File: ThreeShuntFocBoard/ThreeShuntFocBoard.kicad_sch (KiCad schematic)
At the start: 178 parts, among them J1 Conn_01x05, J10 Conn_01x01, J11 Conn_01x01, J12 Conn_01x01, J13 Conn_01x01, J14 Conn_01x01, J15 Conn_01x01, J16 Conn_01x01, J17 Conn_01x01, J18 Conn_01x01, J2 Conn_01x01, J3 Conn_01x03, J5 Conn_01x05, J6 Conn_01x01, J7 Conn_02x03_Odd_Even, J8 Conn_01x01, J9 Conn_01x01, Q1 MMBT5551L, Q10 IRF540N, Q11 MMBT5551L, Q12 SS8050, Q13 SS8550, Q14 SS8550, Q15 SS8550, Q16 SS8550, Q17 IRF540N, Q18 IRF540N, Q19 IRF540N, Q2 SS8050, Q20 IRF540N, Q21 MMBT5551L, Q22 SS8050, Q23 SS8550, Q24 SS8550, Q25 SS8550, Q26 SS8550, Q27 IRF540N, Q28 IRF540N, Q29 IRF540N, Q3 SS8550, Q30 IRF540N, Q31 AOD2146, Q4 SS8550, Q5 SS8550, Q6 SS8550, Q7 IRF540N, Q8 IRF540N, Q9 IRF540N, U1 TX4131L_ESOP8, U2 AMS1117

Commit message: Only PhaseA inverter section is implemented : need to review
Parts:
- removed C1, C11, C17, C9: 100nF, Footprints:C_0603, symbol Device:C_Small
- removed C10, C14, C20: 47uF 63V, BLDC:220uF63V, symbol Device:C_Polarized_US
- removed C12, C13, C18, C19, C4, C5, C6, C7, C8: 10nF, Footprints:C_0603, symbol Device:C_Small
- removed C15, C21: 220uF 80V, Footprints:220uF_80VDC, symbol Device:C_Polarized_US
- removed C16, C22, C31: 104J 100V, Footprints:104J_100V, symbol Device:C
- removed C2, C3: 470uF 80V, Footprints:220uF_80VDC, symbol Device:C_Polarized_US
- removed C23: 47uF 160V_UVR2C470MHD1TO, Footprints:47uF_25V, symbol Device:C_Polarized_US
- removed C24: 100nF_200V, Footprints:0.1uF200V, symbol Device:C_Small
- removed C25: 2.2uF_0805, Footprints:1206_C, symbol Device:C_Small
- removed C26: 4.7uF 25V, Footprints:C_0603, symbol Device:C_Small
- removed C27: 220uF 25V, Footprints:220uF 25V, symbol Device:C_Polarized_US
- removed C28: 100nF 25V, Footprints:C_0603, symbol Device:C_Small
- removed C29: 100uF 25V, Footprints:100uF 25V_2917, symbol Device:C_Polarized_US
- removed C30: 22uF 10V, Footprints:22uF 10V, symbol Device:C_Polarized_US
- removed D1, D4, D7: 1N4007, BLDC:ZenerDiode_S1M, symbol Diode:1N4007
- removed D10: BZT52C15-13-F, Footprints:BZT52C15-13-F, symbol Diode:BZT52Bxx
- removed D11: 1N4148W-7-F_SOD123, Footprints:SOD_123_v1, symbol Diode:1N4148
- removed D12, D13: D_Schottky, Footprints:SS24-HF, symbol Device:D_Schottky
- removed D14, D15: LED, Footprints:LED_0603, symbol Device:LED
- removed D2, D3, D5, D6, D8, D9: 1N4148, Footprints:SOD_123_v1, symbol Diode:1N4148
- removed FB1: FerriteBead, Footprints:BLM21SP471SN1D, symbol Device:FerriteBead
- removed FB2, FB3, FB4: BLM21SP471SN1D, Footprints:BLM21SP471SN1D, symbol Device:FerriteBead
- removed J1, J5: Conn_01x05, BLDC:Socket_Strip_Straight_1x05_Pitch2.54mm, symbol Connector_Generic:Conn_01x05
- removed J10, J11, J12, J13, J14, J15, J16, J17, J18, J2, J6, J8, J9: Conn_01x01, Footprints:Powe_pad, symbol Connector_Generic:Conn_01x01
- removed J3: Conn_01x03, BLDC:Socket_Strip_Straight_1x03_Pitch2.54mm, symbol Connector_Generic:Conn_01x03
- removed J7: Conn_02x03_Odd_Even, BLDC:Socket_Strip_Straight_oddeven_2x06_Pitch2.54mm, symbol Connector_Generic:Conn_02x03_Odd_Even
- removed JP1, JP2: Jumper_2_Open, Footprints:104J_100V, symbol Jumper:Jumper_2_Open
- removed L1: Fixed Inductors 47uH, Footprints:47uH_Inductor, symbol Device:L
- removed Q1, Q11, Q21: MMBT5551L, Footprints:SOT-23_v1, symbol Transistor_BJT:MMBT5551L
- removed Q10, Q17, Q18, Q19, Q20, Q27, Q28, Q29, Q30, Q7, Q8, Q9: IRF540N, BLDC:TO-220-3_Vertical, symbol Transistor_FET:IRF540N
- removed Q12, Q2, Q22: SS8050, Footprints:SOT-23_v1, symbol Transistor_BJT:S8050
- removed Q13, Q14, Q15, Q16, Q23, Q24, Q25, Q26, Q3, Q4, Q5, Q6: SS8550, Footprints:SOT-23_v1, symbol Transistor_BJT:S8550
- removed Q31: AOD2146, Footprints:AOD4126, symbol Transistor_FET:IRF540N
- removed R1, R25, R5: 0E, Footprints:R_0603, symbol Device:R
- removed R10, R12, R32, R34, R52, R54: 510E, Footprints:R_0603, symbol Device:R
- removed R11, R13, R17, R18, R2, R27, R28, R29, R3, R30, R31, R33, R35, R36, R37, R4, R45, R46, R48, R49, R50, R51, R53, R55, R56, R57, R6, R7, R8, R9: 2.2K, Footprints:R_0603, symbol Device:R
- removed R14, R15, R16: 3.3K, Footprints:R_0603, symbol Device:R
- removed R19, R38, R58: 560R, Footprints:R_0603, symbol Device:R
- removed R20, R39, R59: 560E, Footprints:R_0603, symbol Device:R
- removed R21, R22, R23, R24, R40, R41, R42, R43, R60, R61, R62, R63: 6.9E, Footprints:R_0603, symbol Device:R
- removed R26, R44, R64: 10K, Footprints:1206_R, symbol Device:R
- removed R47: 51K, Footprints:1206_R, symbol Device:R
- removed R65: 100R, Footprints:R_0603, symbol Device:R
- removed R66, R68: 1.8K, Footprints:R_0603, symbol Device:R
- removed R67, R69: 56K, Footprints:R_0603, symbol Device:R
- removed R70, R71, R72: 0.1R 0.25W, Footprints:0.1R 0.25W, symbol Device:R
- removed R73: 22K, Footprints:R_0603, symbol Device:R
- removed R74: 1.69K, Footprints:R_0603, symbol Device:R
- removed R75: 1K, Footprints:R_0603, symbol Device:R
- removed U1: TX4131L_ESOP8, Footprints:TX4131L_ESOP8, symbol Symbol_lib:TX4131L_ESOP8
- removed U2: AMS1117, Footprints:AMS1117 SOT-223, symbol Regulator_Linear:AMS1117
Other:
- added sheet DigitalSection (DigitalSection.kicad_sch)
- added sheet PhaseA (Inverter.kicad_sch)
- added sheet PowerSupply (PowerSupply.kicad_sch)
- note removed: "+12VDC Supply"
- note removed: "+5VDC Supply"
- note removed: "10KOhm_1 1206"
- note removed: "CHOKE KIND OF CAPACITOR"
- note removed: "DIGITAL_ GND"
- note removed: "INVERTER_SECTION"
- note removed: "PWM SINGALS"
- note removed: "Place this capacitor near to phaseA DRAIN Side"
- note removed: "SUPPLY_CONNECTION"
- note removed: "Test-point"

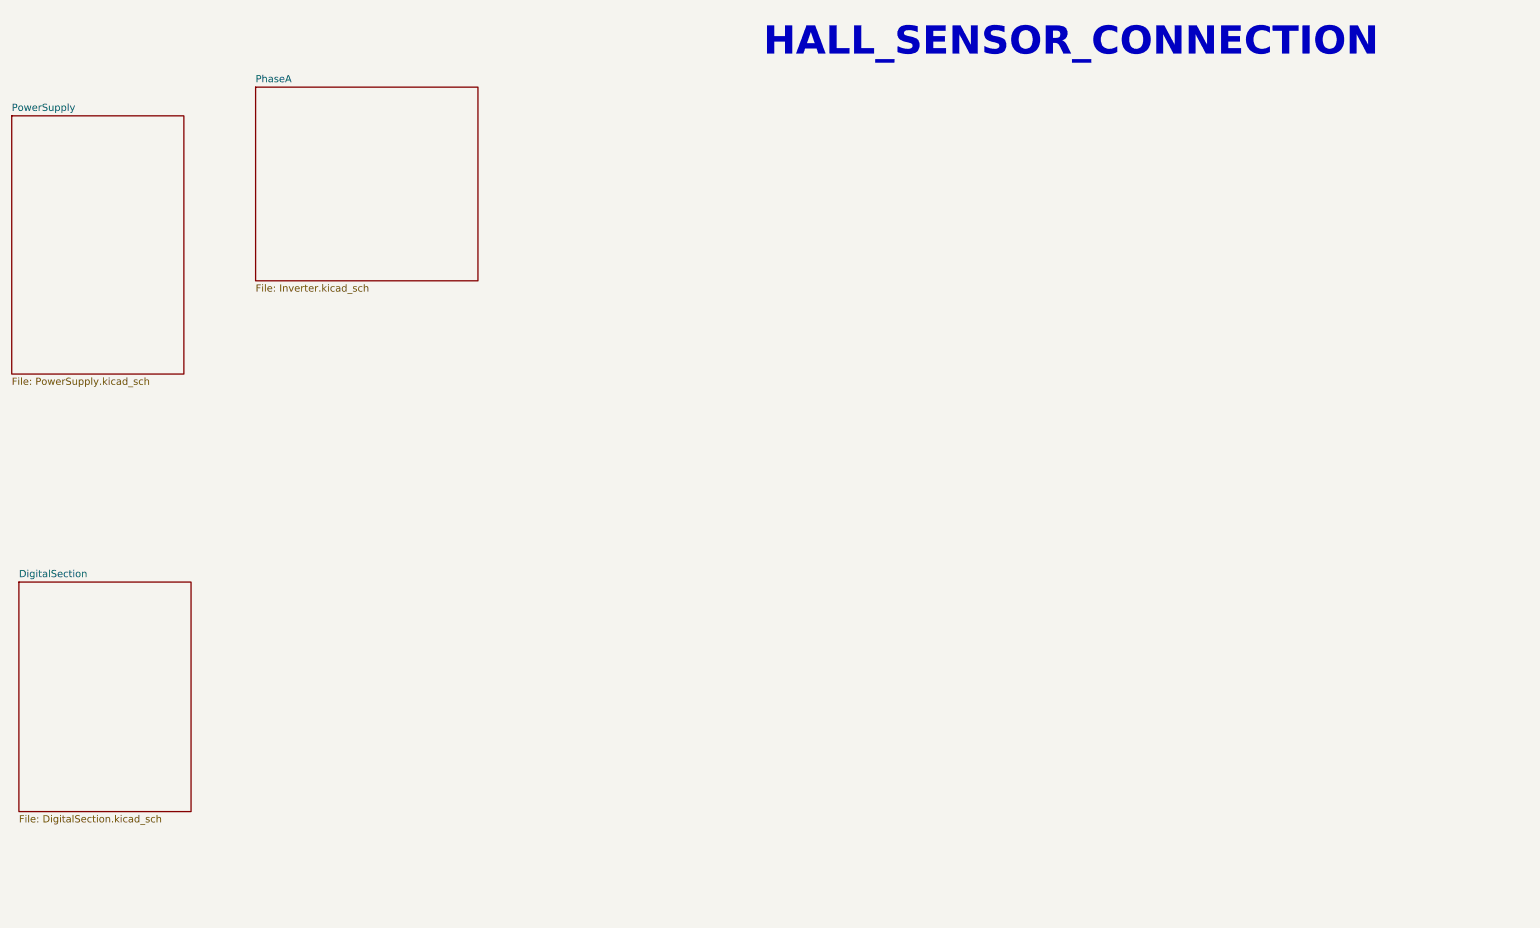
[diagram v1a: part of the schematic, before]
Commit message: commit 2:  Updated Power Supply, Safety Fuse, Phase Design, and Hall Sensor Circuit
for more details read ChangesDetial.txt in same folder.
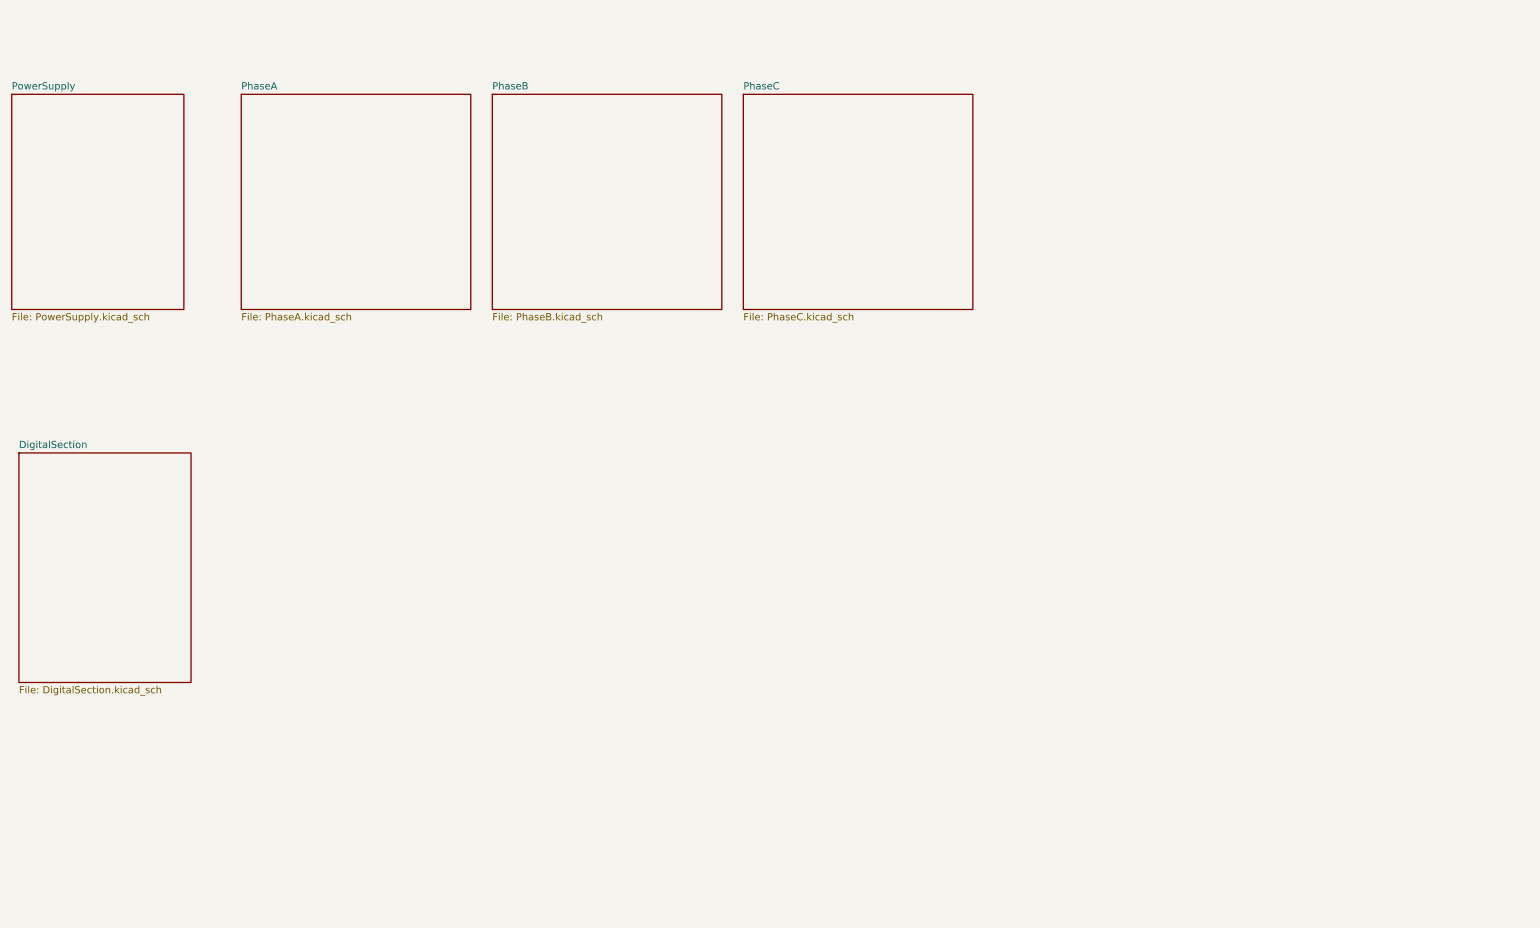
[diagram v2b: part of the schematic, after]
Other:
- added sheet PhaseB (PhaseB.kicad_sch)
- added sheet PhaseC (PhaseC.kicad_sch)
- sheet PhaseA: file Inverter.kicad_sch -> PhaseA.kicad_sch
- note removed: "HALL_SENSOR_CONNECTION"
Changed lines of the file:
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@@
-		)
-	)
-	(text "HALL_SENSOR_CONNECTION"
-		(exclude_from_sim no)
-		(at 157.226 24.13 0)
-		(effects
-			(font
-				(size 5 5)
-				(bold yes)
-			)
-			(justify left bottom)
 		)
 	)
 	(sheet
-		(at 67.31 29.21)
-		(size 39.37 34.29)
+		(at 109.22 30.48)
+		(size 40.64 38.1)
 		(fields_autoplaced yes)
 		(stroke
@@
 			(color 0 0 0 0.0000)
 		)
-		(property "Sheetname" "PhaseA"
-			(at 67.31 28.4984 0)
+		(property "Sheetname" "PhaseB"
+			(at 109.22 29.7684 0)
 			(effects
 				(font
@@
 			)
 		)
-		(property "Sheetfile" "Inverter.kicad_sch"
-			(at 67.31 64.0846 0)
+		(property "Sheetfile" "PhaseB.kicad_sch"
+			(at 109.22 69.1646 0)
 			(effects
 				(font
@@
 			(project "ThreeShuntFocBoard"
 				(path "/b106e329-9ec1-4501-b5a0-9c80558ba634"
-					(page "3")
+					(page "5")
 				)
 			)
@@
 	)
 	(sheet
-		(at 24.13 34.29)
-		(size 30.48 45.72)
+		(at 64.77 30.48)
+		(size 40.64 38.1)
+		(fields_autoplaced yes)
+		(stroke
+			(width 0.1524)
+			(type solid)
+		)
+		(fill
+			(color 0 0 0 0.0000)
+		)
+		(property "Sheetname" "PhaseA"
+			(at 64.77 29.7684 0)
+			(effects
+				(font
+					(size 1.27 1.27)
+				)
+				(justify left bottom)
+			)
+		)
+		(property "Sheetfile" "PhaseA.kicad_sch"
+			(at 64.77 69.1646 0)
+			(effects
+				(font
+					(size 1.27 1.27)
+				)
+				(justify left top)
+			)
+		)
+		(instances
+			(project "ThreeShuntFocBoard"
+				(path "/b106e329-9ec1-4501-b5a0-9c80558ba634"
+					(page "6")
+				)
+			)
+		)
+	)
+	(sheet
+		(at 24.13 30.48)
+		(size 30.48 38.1)
 		(fields_autoplaced yes)
 		(stroke
@@
 		)
 		(property "Sheetname" "PowerSupply"
-			(at 24.13 33.5784 0)
+			(at 24.13 29.7684 0)
 			(effects
 				(font
@@
 		)
 		(property "Sheetfile" "PowerSupply.kicad_sch"
-			(at 24.13 80.5946 0)
+			(at 24.13 69.1646 0)
 			(effects
 				(font
@@
 	)
 	(sheet
-		(at 25.4 116.84)
+		(at 25.4 93.98)
 		(size 30.48 40.64)
 		(fields_autoplaced yes)
@@
 		)
 		(property "Sheetname" "DigitalSection"
-			(at 25.4 116.1284 0)
+			(at 25.4 93.2684 0)
 			(effects
 				(font
@@
 		)
 		(property "Sheetfile" "DigitalSection.kicad_sch"
-			(at 25.4 158.0646 0)
+			(at 25.4 135.2046 0)
 			(effects
 				(font
@@
 				)
 			)
+		)
+	)
+	(sheet
+		(at 153.67 30.48)
+		(size 40.64 38.1)
+		(fields_autoplaced yes)
+		(stroke
+			(width 0.1524)
+			(type solid)
+		)
+		(fill
+			(color 0 0 0 0.0000)
+		)
+		(property "Sheetname" "PhaseC"
+			(at 153.67 29.7684 0)
+			(effects
+				(font
+					(size 1.27 1.27)
+				)
+				(justify left bottom)
+			)
+		)
+		(property "Sheetfile" "PhaseC.kicad_sch"
+			(at 153.67 69.1646 0)
+			(effects
+				(font
+					(size 1.27 1.27)
+				)
+				(justify left top)
+			)
+		)
+		(instances
+			(project "ThreeShuntFocBoard"
+				(path "/b106e329-9ec1-4501-b5a0-9c80558ba634"
+					(page "6")
+				)
+			)
